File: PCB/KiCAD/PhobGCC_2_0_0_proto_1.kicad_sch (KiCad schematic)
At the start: 110 parts, among them J1 Conn_01x06_Female, J11 Conn_01x02, J14 Conn_01x06, J15 Conn_01x06, J2 Conn_01x02, J3 Conn_01x02, J4 Conn_01x01, J5 Rumble, J6 Conn_01x06, J8 USB_B_Micro, Q1 Q_NMOS_GSD, Q2 Q_PMOS_GDS, Q3 Q_NMOS_GSD, SW1 A, SW10 Dup, SW11 Dright, SW12 Ddown, SW2 B, SW3 X, SW4 Y, SW5 Start, SW6 L, SW7 R, SW8 Z, SW9 Dleft, U1 MCP3202, U10 DRV5055A3xDBZxQ1, U11 DRV5055A3xDBZxQ1, U12 USBLC6-2P6, U13 USBLC6-2P6, U2 Stickbox_Assembly_Main, U3 MCP3202, U4 DRV5055A3xDBZxQ1, U5 Stickbox_Assembly_CStick, U6 AMS1117-3.3, U7 W25Q128JVS, U8 RP2040, U9 DRV5055A3xDBZxQ1, Y1 Crystal_GND24

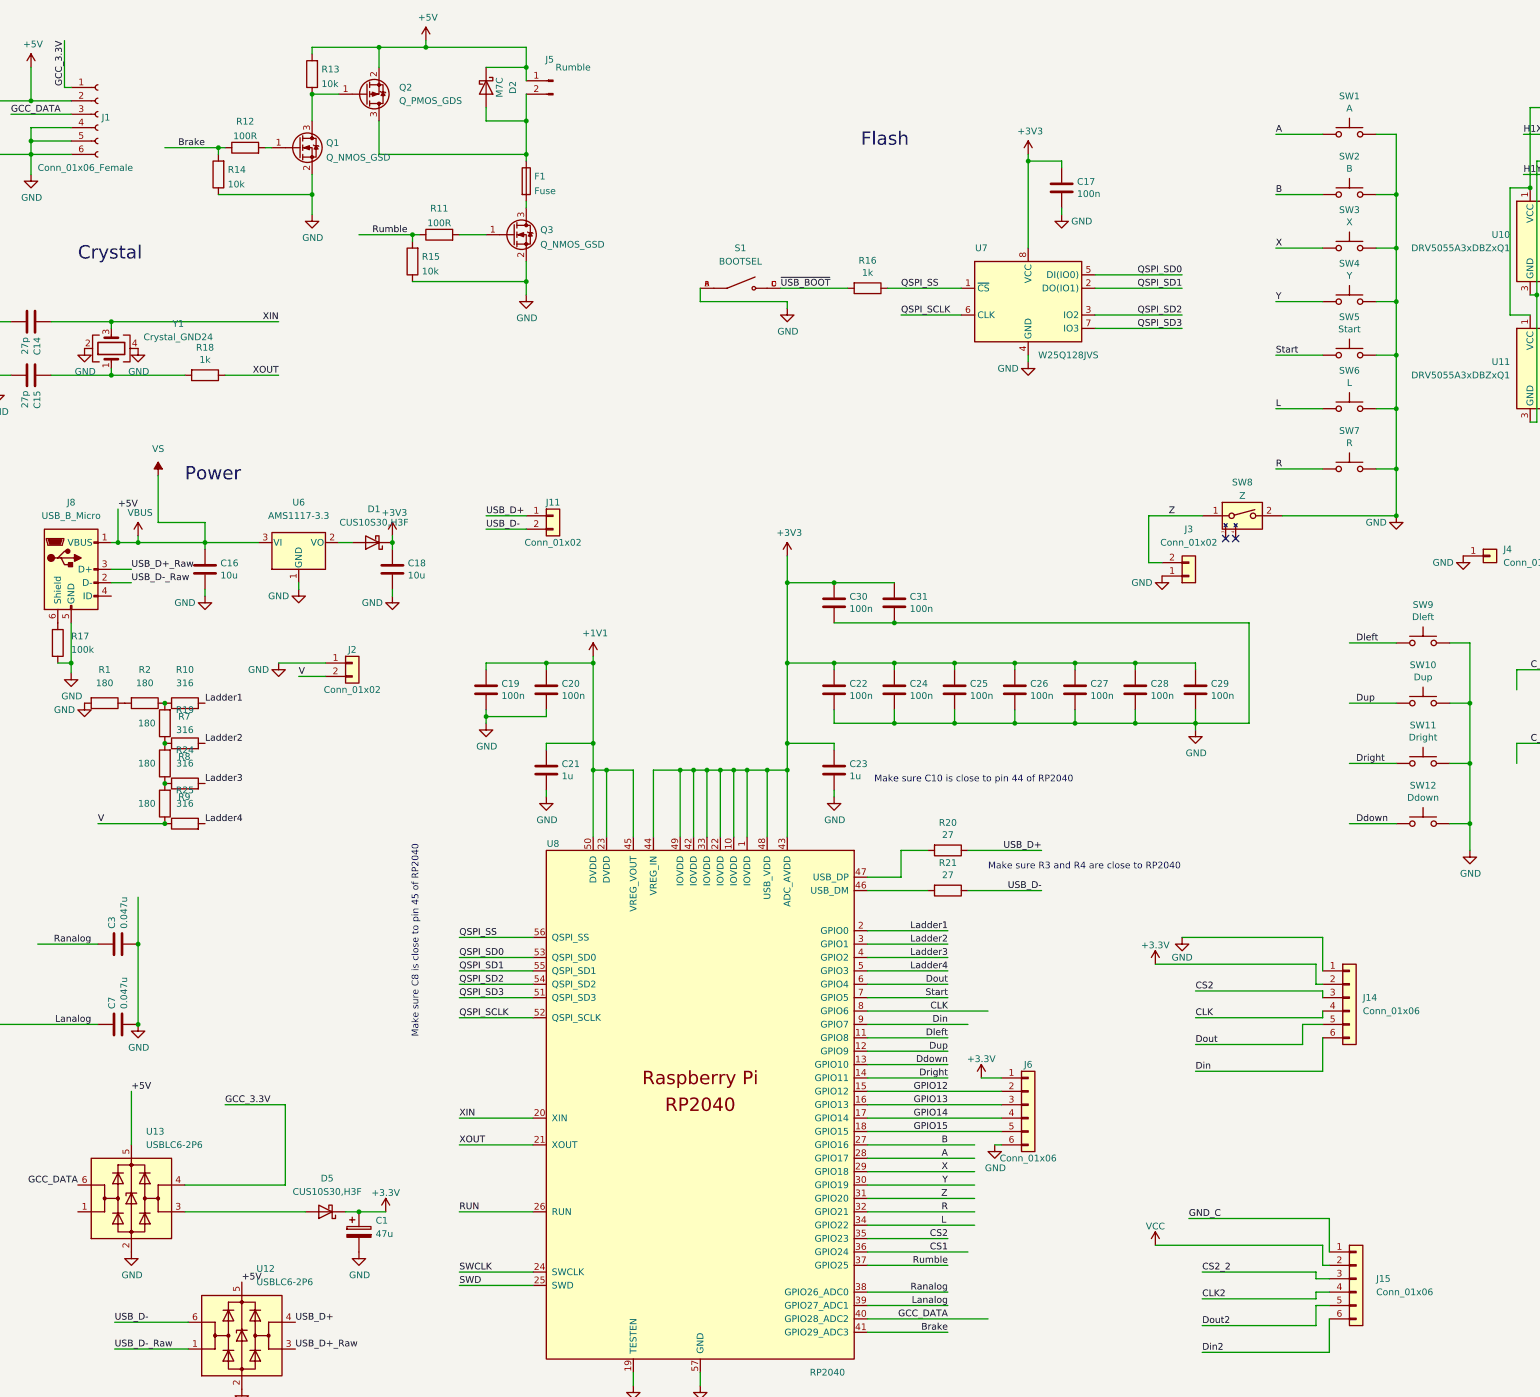
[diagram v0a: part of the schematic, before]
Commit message: Changes location of C-stick header Changes C-stick header pitch to 2.54 mm (100 mil)
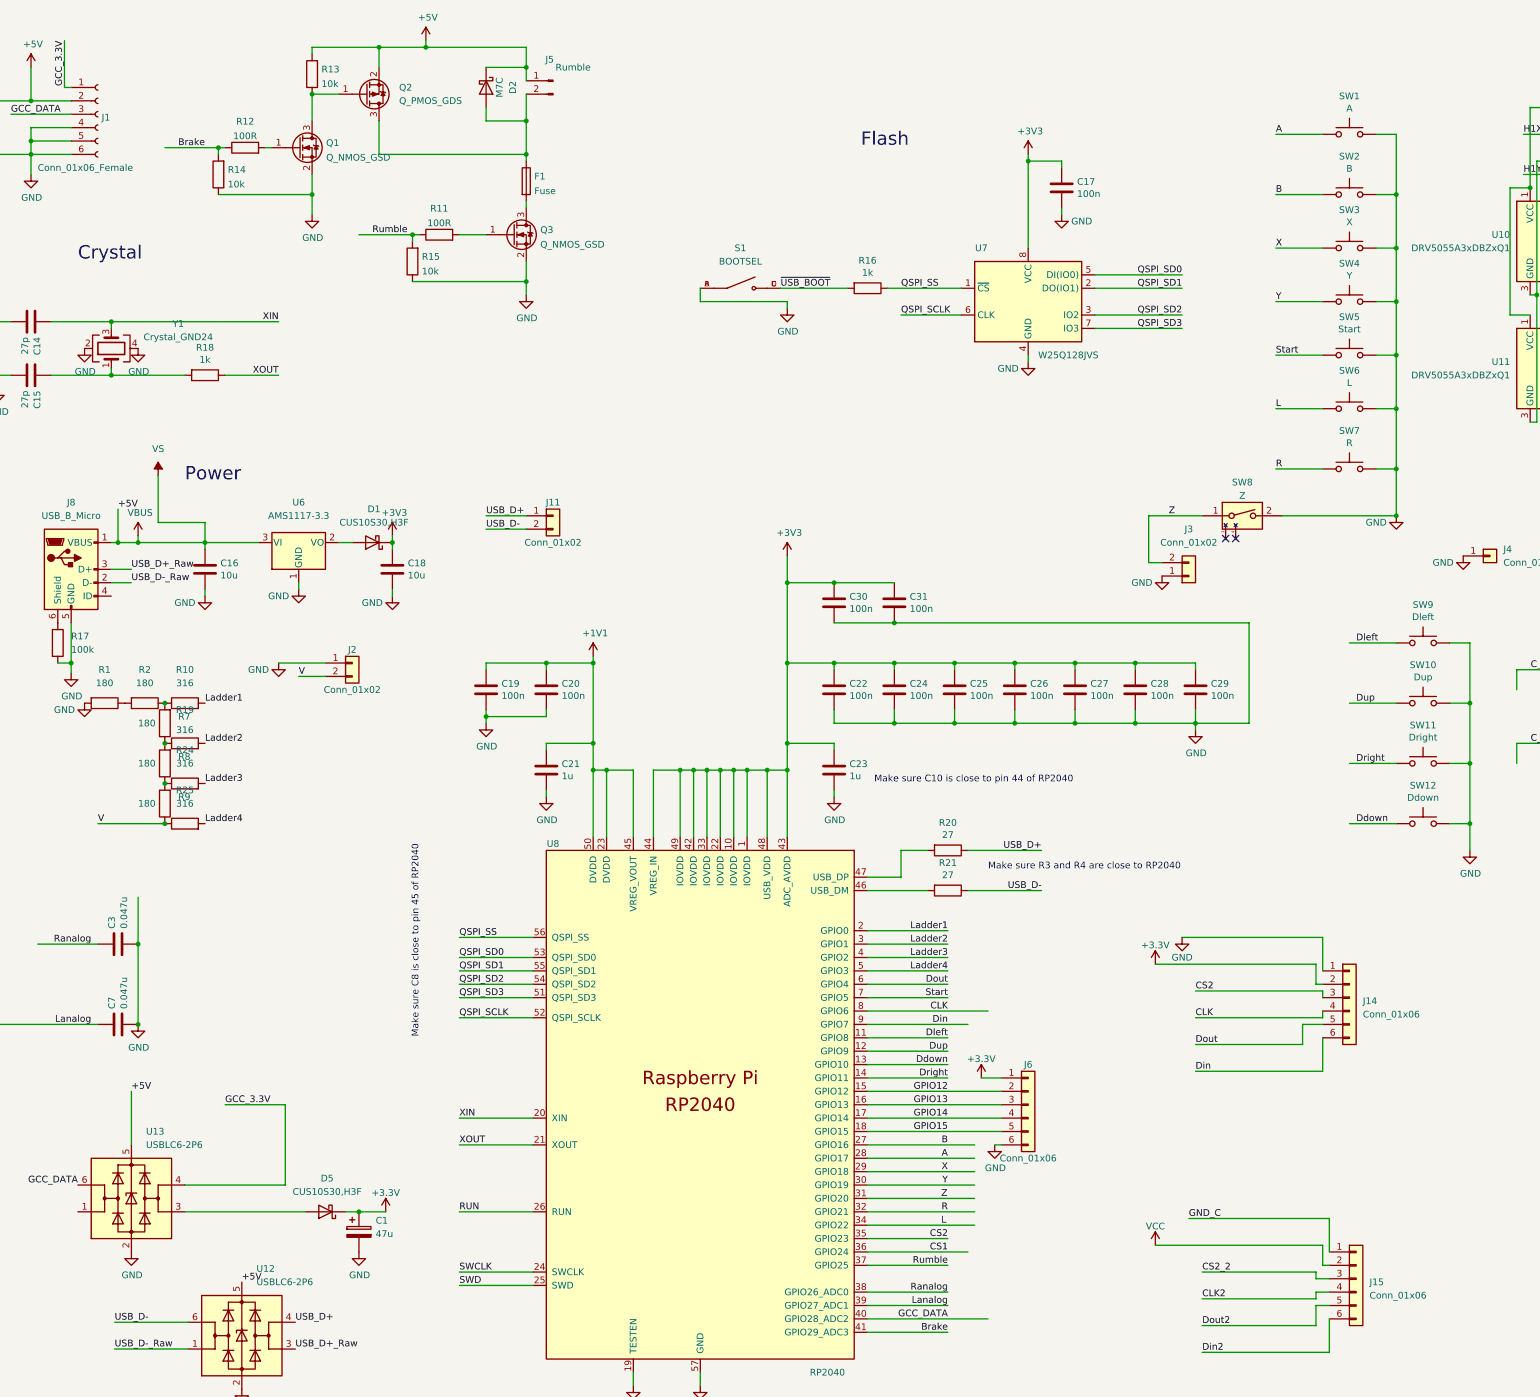
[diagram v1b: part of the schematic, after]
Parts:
- J14: footprint PhobGCC_2_0_0_footprints:PinSocket_1x06_P2.00mm_Vertical -> Connector_PinHeader_2.54mm:PinHeader_1x06_P2.54mm_Vertical
- J15: footprint PhobGCC_2_0_0_footprints:PinSocket_1x06_P2.00mm_Vertical -> Connector_PinSocket_2.54mm:PinSocket_1x06_P2.54mm_Vertical
